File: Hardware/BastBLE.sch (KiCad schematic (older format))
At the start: 33 parts, among them J1 Battery, J2 SWD, J3 Conn_left, J4 Conn_right, P1 USB_C_Plug_USB2.0, Q1 DMG3415U-7, SW1 RESET, U1 AP2112K-3.3, U2 E73-2G4M08S1C, U3 MCP73831-2-OT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

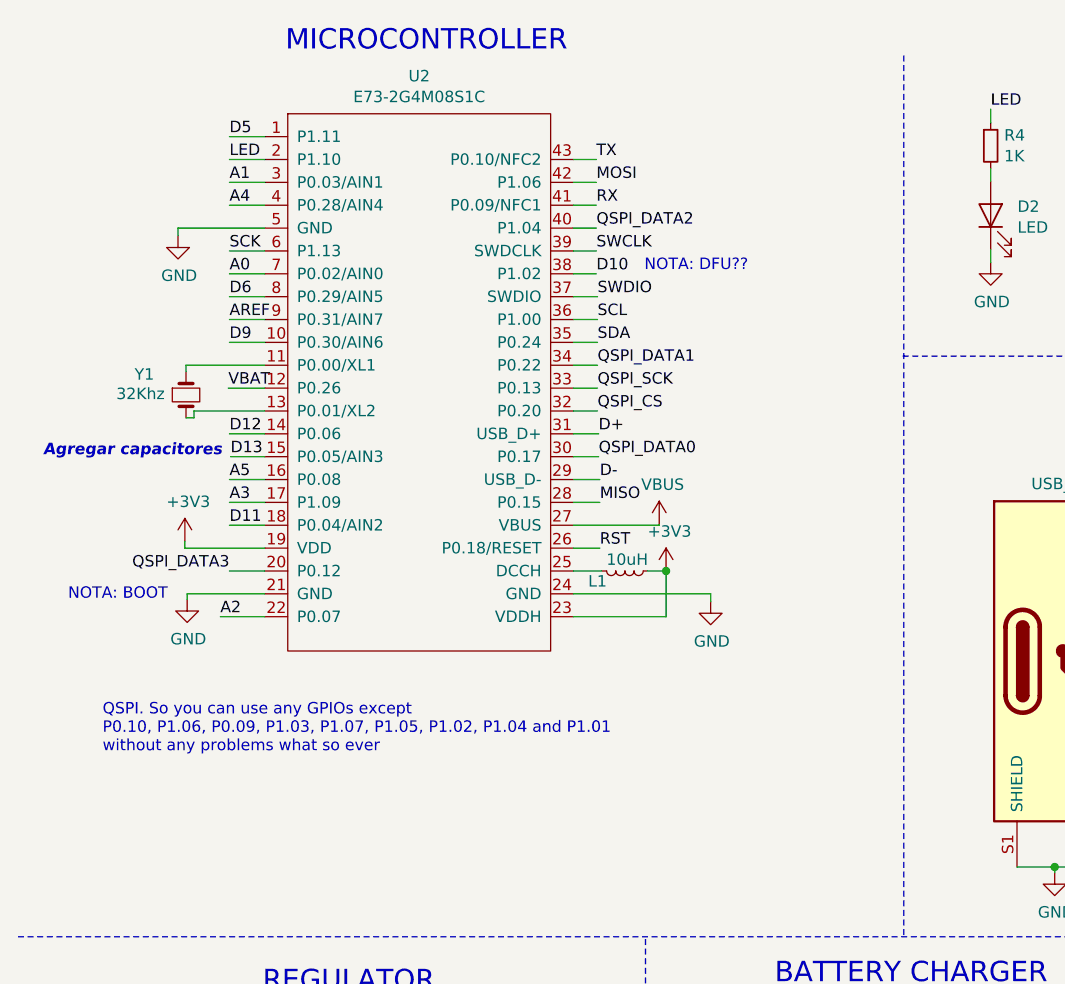
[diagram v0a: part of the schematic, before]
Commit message: add crystal and fix analogs
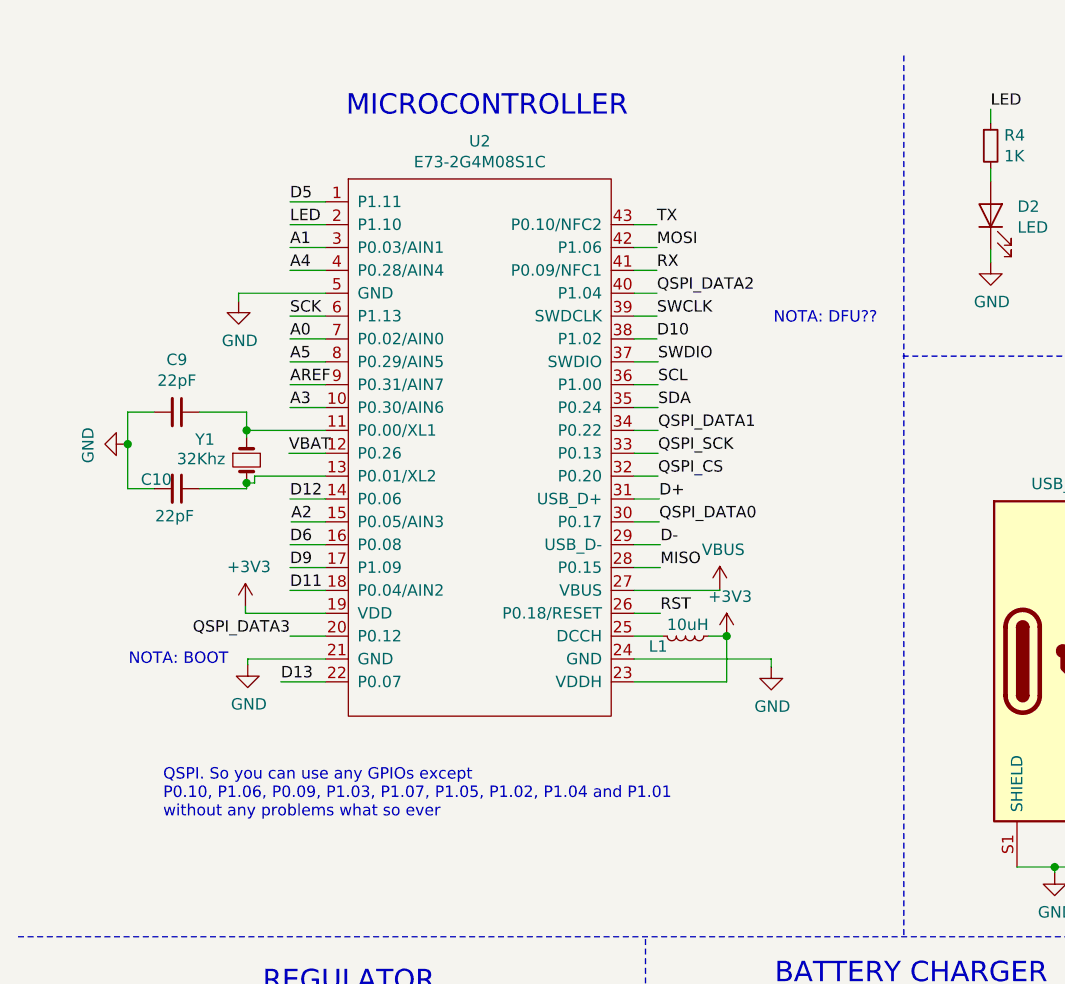
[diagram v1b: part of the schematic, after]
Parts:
- added C10, C9: 22pF, symbol Device:C_Small
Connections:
- net A2: now also U2.15 (P0.05/AIN3); no longer U2.22 (P0.07)
- net A3: now also U2.10 (P0.30/AIN6); no longer U2.17 (P1.09)
- net A5: now also U2.8 (P0.29/AIN5); no longer U2.16 (P0.08)
- net D13: now also U2.22 (P0.07); no longer U2.15 (P0.05/AIN3)
- net D6: now also U2.16 (P0.08); no longer U2.8 (P0.29/AIN5)
- net D9: now also U2.17 (P1.09); no longer U2.10 (P0.30/AIN6)
- net GND: now also C10.2, C9.2
- net at U2.11 (P0.00/XL1), Y1.1: now also C9.1
- net at U2.13 (P0.01/XL2), Y1.2: now also C10.1
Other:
- note removed: "Agregar capacitores"
- moved on the sheet: L1, U2, Y1

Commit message: add footprint and netlist
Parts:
- C10, C9: footprint (none) -> Capacitor_SMD:C_0603_1608Metric_Pad1.05x0.95mm_HandSolder
- D2, D3: footprint LED_SMD:LED_0603_1608Metric_Pad1.05x0.95mm_HandSolder -> LED_SMD:LED_0805_2012Metric
- Y1: footprint Crystal:Crystal_SMD_SeikoEpson_MC146-4Pin_6.7x1.5mm -> Crystal:Crystal_SMD_3215-2Pin_3.2x1.5mm
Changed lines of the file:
@@
 EESchema Schematic File Version 4
+LIBS:BastBLE-cache
 EELAYER 30 0
 EELAYER END
@@
 F 0 "Y1" V 1375 2015 50  0000 L CNN
 F 1 "32Khz" V 1460 1935 50  0000 L CNN
-F 2 "Crystal:Crystal_SMD_SeikoEpson_MC146-4Pin_6.7x1.5mm" H 1465 2240 50  0001 C CNN
+F 2 "Crystal:Crystal_SMD_3215-2Pin_3.2x1.5mm" H 1465 2240 50  0001 C CNN
 F 3 "~" H 1465 2240 50  0001 C CNN
 	1    1465 2240
@@
 F 0 "D2" V 4759 1053 50  0000 R CNN
 F 1 "LED" V 4668 1053 50  0000 R CNN
-F 2 "LED_SMD:LED_0603_1608Metric_Pad1.05x0.95mm_HandSolder" H 4720 1170 50  0001 C CNN
+F 2 "LED_SMD:LED_0805_2012Metric" H 4720 1170 50  0001 C CNN
 F 3 "~" H 4720 1170 50  0001 C CNN
 	1    4720 1170
@@
 F 0 "D3" H 5178 5621 50  0000 C CNN
 F 1 "LED" H 5178 5530 50  0000 C CNN
-F 2 "LED_SMD:LED_0603_1608Metric_Pad1.05x0.95mm_HandSolder" H 5185 5405 50  0001 C CNN
+F 2 "LED_SMD:LED_0805_2012Metric" H 5185 5405 50  0001 C CNN
 F 3 "~" H 5185 5405 50  0001 C CNN
 	1    5185 5405
@@
 F 0 "C10" V 1120 2275 50  0000 C CNN
 F 1 "22pF" V 1280 2355 50  0000 C CNN
-F 2 "" H 1160 2365 50  0001 C CNN
+F 2 "Capacitor_SMD:C_0603_1608Metric_Pad1.05x0.95mm_HandSolder" H 1160 2365 50  0001 C CNN
 F 3 "~" H 1160 2365 50  0001 C CNN
 	1    1160 2365
@@
 F 0 "C9" V 931 2030 50  0000 C CNN
 F 1 "22pF" V 1022 2030 50  0000 C CNN
-F 2 "" H 1160 2030 50  0001 C CNN
+F 2 "Capacitor_SMD:C_0603_1608Metric_Pad1.05x0.95mm_HandSolder" H 1160 2030 50  0001 C CNN
 F 3 "~" H 1160 2030 50  0001 C CNN
 	1    1160 2030

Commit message: C6 VBUS
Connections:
- net +3V3: no longer C6.1
- net VBUS: now also C6.1
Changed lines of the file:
@@
-$EndComp
-$Comp
-L power:+3V3 #PWR031
-U 1 1 5E3E7D7A
-P 6005 920
-F 0 "#PWR031" H 6005 770 50  0001 C CNN
-F 1 "+3V3" H 6020 1093 50  0000 C CNN
-F 2 "" H 6005 920 50  0001 C CNN
-F 3 "" H 6005 920 50  0001 C CNN
-	1    6005 920
-	1    0    0    -1
 $EndComp
 $Comp
@@
 Text Notes 3770 1650 0    50   ~ 0
 NOTA: DFU??
+$Comp
+L power:VBUS #PWR?
+U 1 1 5EBF05F5
+P 6005 920
+F 0 "#PWR?" H 6005 770 50  0001 C CNN
+F 1 "VBUS" H 6020 1093 50  0000 C CNN
+F 2 "" H 6005 920 50  0001 C CNN
+F 3 "" H 6005 920 50  0001 C CNN
+	1    6005 920
+	1    0    0    -1
+$EndComp
 $EndSCHEMATC

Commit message: D- D+
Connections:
- net D11: now also U2.17 (P1.09); no longer U2.18 (P0.04/AIN2)
- net D12: now also U2.16 (P0.08); no longer U2.14 (P0.06)
- net D5: now also U2.6 (P1.13); no longer U2.1 (P1.11)
- net D6: now also U2.14 (P0.06); no longer U2.16 (P0.08)
- net D9: now also U2.18 (P0.04/AIN2); no longer U2.17 (P1.09)
- net SCK: now also U2.1 (P1.11); no longer U2.6 (P1.13)
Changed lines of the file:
@@
 Text Label 3260 1410 0    50   ~ 0
 RX
-Text Label 1655 2410 0    50   ~ 0
+Text Label 1655 2610 0    50   ~ 0
 D12
 Wire Wire Line
@@
 Text Label 3260 1210 0    50   ~ 0
 TX
-Text Label 1655 2710 0    50   ~ 0
+Text Label 1655 2810 0    50   ~ 0
 D9
 Text Label 3270 2510 0    50   ~ 0
@@
 Text Label 3260 1310 0    50   ~ 0
 MOSI
-Text Label 1655 1610 0    50   ~ 0
+Text Label 1655 1110 0    50   ~ 0
 SCK
 Text Notes 1100 3810 0    50   ~ 0
@@
 Text Notes 6040 4595 0    89   ~ 0
 SWD CONN
-Text Label 1655 1110 0    50   ~ 0
-D5
-Text Label 1655 2610 0    50   ~ 0
+Text Label 1655 2410 0    50   ~ 0
 D6
 Text Label 3260 1710 0    50   ~ 0
@@
 Text Label 3260 1610 0    50   ~ 0
 SWCLK
-Text Label 1655 2810 0    50   ~ 0
+Text Label 1655 2710 0    50   ~ 0
 D11
 Text Label 1660 2510 0    50   ~ 0
@@
 NOTA: DFU??
 $Comp
-L power:VBUS #PWR?
+L power:VBUS #PWR0101
 U 1 1 5EBF05F5
 P 6005 920
-F 0 "#PWR?" H 6005 770 50  0001 C CNN
+F 0 "#PWR0101" H 6005 770 50  0001 C CNN
 F 1 "VBUS" H 6020 1093 50  0000 C CNN
 F 2 "" H 6005 920 50  0001 C CNN
@@
 	1    0    0    -1
 $EndComp
+Text Label 1655 1610 0    50   ~ 0
+D5
 $EndSCHEMATC

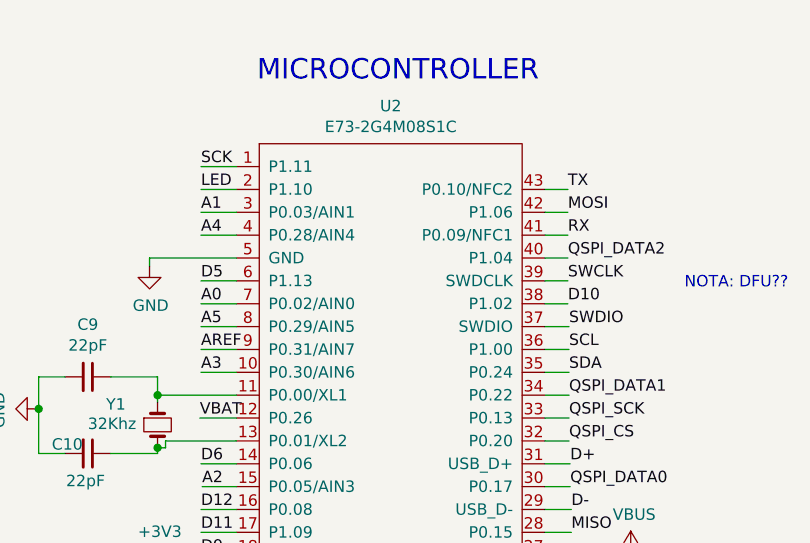
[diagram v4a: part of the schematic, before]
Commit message: change pin SDA SCL
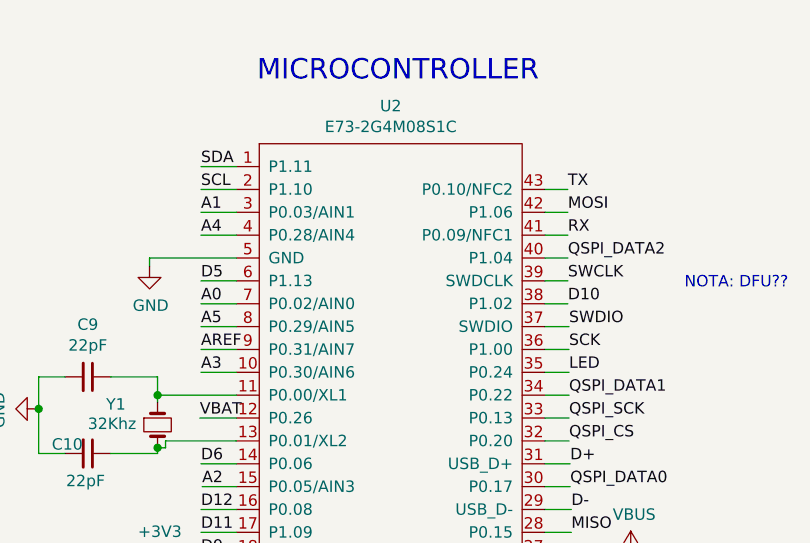
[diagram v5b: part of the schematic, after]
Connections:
- net LED: now also U2.35 (P0.24); no longer U2.2 (P1.10)
- net SCK: now also U2.36 (P1.00); no longer U2.1 (P1.11)
- net SCL: now also U2.2 (P1.10); no longer U2.36 (P1.00)
- net SDA: now also U2.1 (P1.11); no longer U2.35 (P0.24)
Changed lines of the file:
@@
 Text Label 1655 1710 0    50   ~ 0
 A0
-Text Label 1655 1210 0    50   ~ 0
+Text Label 3265 2010 0    50   ~ 0
 LED
 Text Label 3260 1410 0    50   ~ 0
@@
 Text Label 3275 2710 0    50   ~ 0
 MISO
-Text Label 3265 2010 0    50   ~ 0
+Text Label 1655 1110 0    50   ~ 0
 SDA
-Text Label 3265 1910 0    50   ~ 0
+Text Label 1655 1210 0    50   ~ 0
 SCL
 Text Label 3265 2310 0    50   ~ 0
@@
 Text Label 3260 1310 0    50   ~ 0
 MOSI
-Text Label 1655 1110 0    50   ~ 0
+Text Label 3265 1910 0    50   ~ 0
 SCK
 Text Notes 1100 3810 0    50   ~ 0

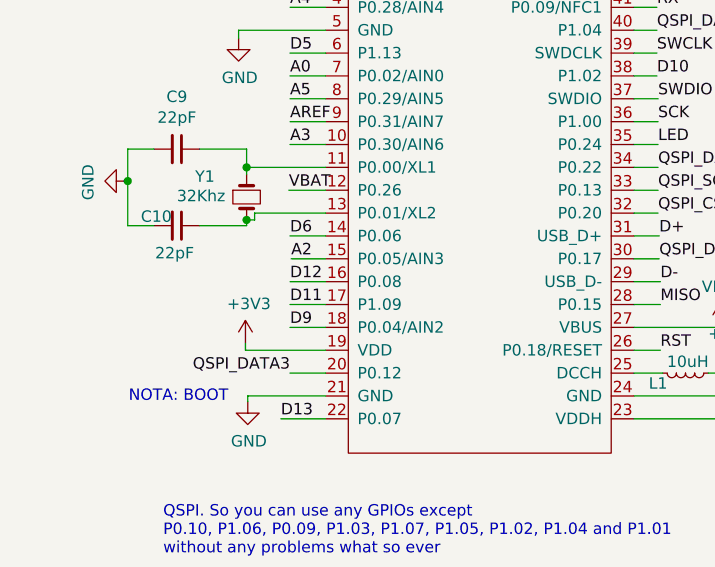
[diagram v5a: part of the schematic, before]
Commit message: fix traces
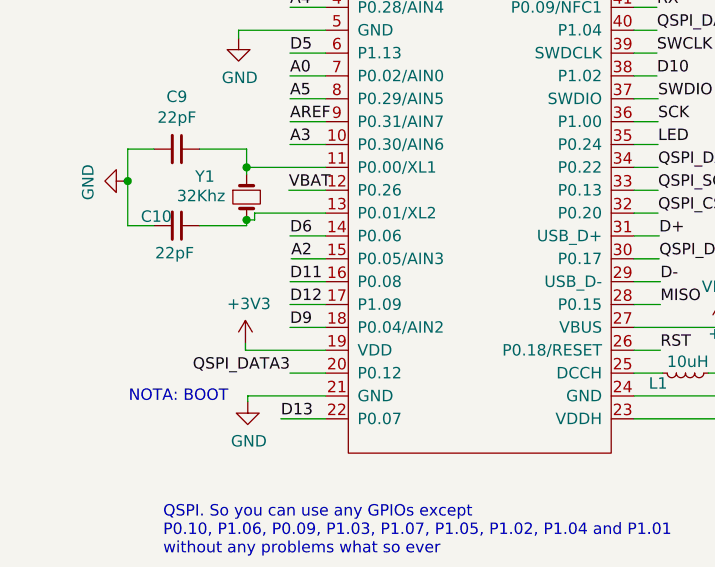
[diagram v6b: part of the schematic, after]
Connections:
- net D11: now also U2.16 (P0.08); no longer U2.17 (P1.09)
- net D12: now also U2.17 (P1.09); no longer U2.16 (P0.08)
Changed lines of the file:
@@
 Text Label 3260 1410 0    50   ~ 0
 RX
-Text Label 1655 2610 0    50   ~ 0
+Text Label 1655 2710 0    50   ~ 0
 D12
 Wire Wire Line
@@
 Text Label 3260 1610 0    50   ~ 0
 SWCLK
-Text Label 1655 2710 0    50   ~ 0
+Text Label 1655 2610 0    50   ~ 0
 D11
 Text Label 1660 2510 0    50   ~ 0

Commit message: first routing
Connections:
- net A1: now also U2.4 (P0.28/AIN4); no longer U2.3 (P0.03/AIN1)
- net A3: now also U2.3 (P0.03/AIN1); no longer U2.10 (P0.30/AIN6)
- net A4: now also U2.10 (P0.30/AIN6); no longer U2.4 (P0.28/AIN4)
- net AREF: no longer J3.3 (Pin_3)
- net D10: now also U2.17 (P1.09); no longer U2.38 (P1.02)
- net D12: now also U2.18 (P0.04/AIN2); no longer U2.17 (P1.09)
- net D5: now also U2.38 (P1.02); no longer U2.6 (P1.13)
- net D6: now also U2.6 (P1.13); no longer U2.14 (P0.06)
- net D9: now also U2.14 (P0.06); no longer U2.18 (P0.04/AIN2)
- net GND: now also J3.3 (Pin_3)
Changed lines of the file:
@@
 EESchema Schematic File Version 4
-LIBS:BastBLE-cache
 EELAYER 30 0
 EELAYER END
@@
 Text Label 3260 1410 0    50   ~ 0
 RX
-Text Label 1655 2710 0    50   ~ 0
+Text Label 1655 2810 0    50   ~ 0
 D12
 Wire Wire Line
 	1615 3210 1810 3210
-Text Label 1655 1310 0    50   ~ 0
+Text Label 1655 1410 0    50   ~ 0
 A1
 Text Label 1655 2010 0    50   ~ 0
-A3
-Text Label 1655 1410 0    50   ~ 0
 A4
 Text Label 1655 1810 0    50   ~ 0
@@
 Text Label 3260 1210 0    50   ~ 0
 TX
-Text Label 1655 2810 0    50   ~ 0
+Text Label 1655 2410 0    50   ~ 0
 D9
 Text Label 3270 2510 0    50   ~ 0
@@
 Wire Wire Line
 	8830 1515 8830 1325
-Wire Wire Line
-	9105 1615 9010 1615
 Wire Wire Line
 	9105 1815 9010 1815
@@
 Text Label 9010 1815 2    50   ~ 0
 A0
-Text Label 9010 1615 2    50   ~ 0
-AREF
 Text Label 9000 1415 2    50   ~ 0
 RST
@@
 Text Notes 6040 4595 0    89   ~ 0
 SWD CONN
-Text Label 1655 2410 0    50   ~ 0
+Text Label 1655 1610 0    50   ~ 0
 D6
-Text Label 3260 1710 0    50   ~ 0
+Text Label 1655 2710 0    50   ~ 0
 D10
 Text Notes 949  3143 0    50   ~ 0
@@
 Text Label 1655 2610 0    50   ~ 0
 D11
-Text Label 1660 2510 0    50   ~ 0
-A2
 $Comp
 L Device:C_Small C10
@@
 	1    0    0    -1
 $EndComp
-Text Label 1655 1610 0    50   ~ 0
+Text Label 3260 1710 0    50   ~ 0
 D5
+Text Label 1660 2510 0    50   ~ 0
+A2
+Text Label 1655 1310 0    50   ~ 0
+A3
+Wire Wire Line
+	8740 1715 8740 1615
+Wire Wire Line
+	8740 1615 9105 1615
+Connection ~ 8740 1715
 $EndSCHEMATC
